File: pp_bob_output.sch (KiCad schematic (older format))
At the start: 24 parts, among them P4 13X2, U1 74LS540, U2 74LVC245, U3 74LS541

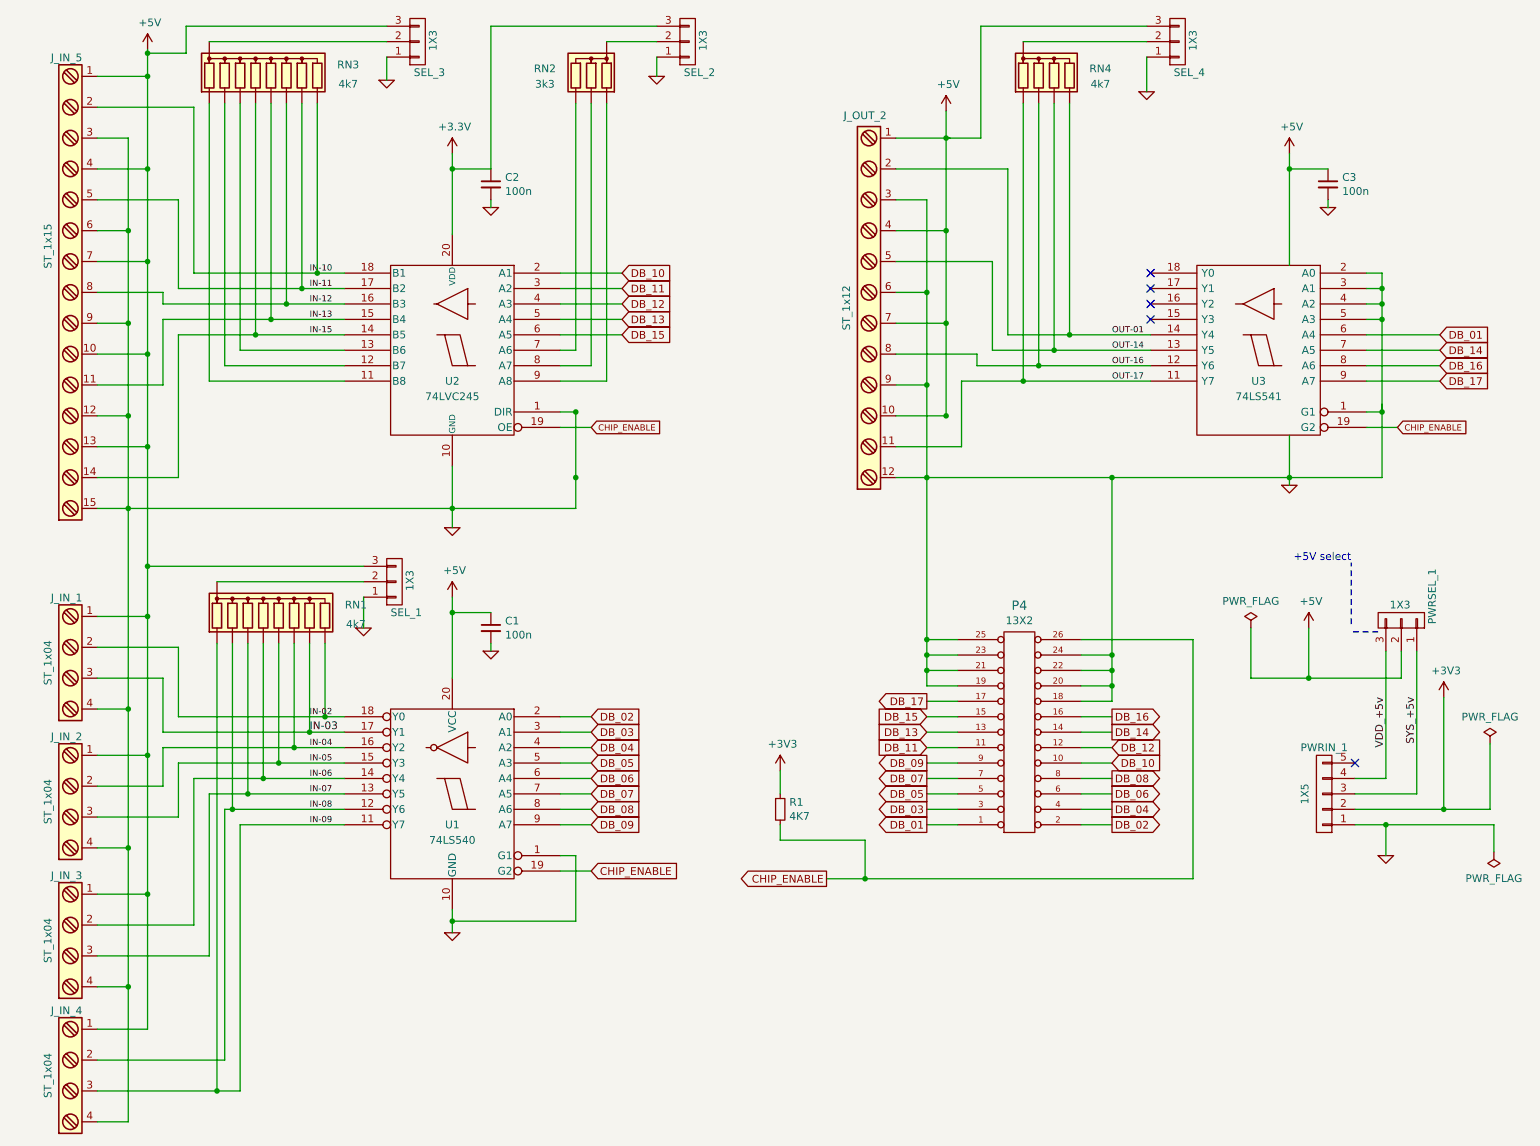
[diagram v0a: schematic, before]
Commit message: Cleaned up schematic
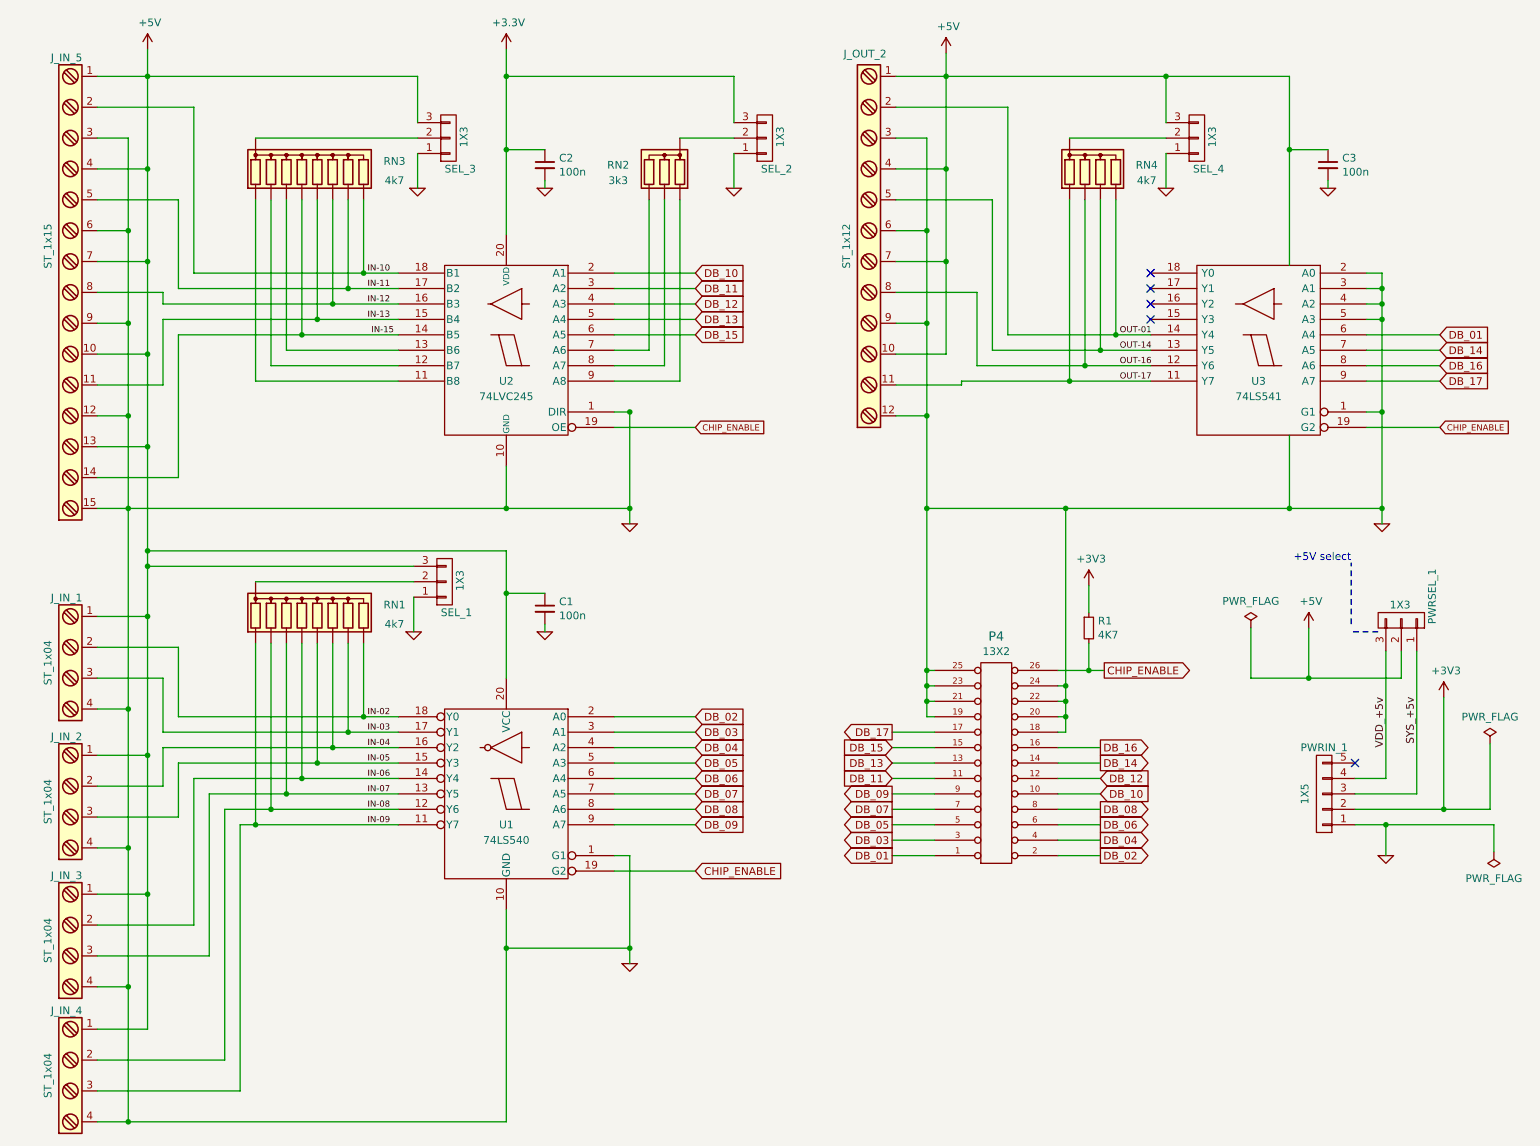
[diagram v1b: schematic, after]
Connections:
- net IN-02: no longer J_IN_1.3, RN1.8 (R7), U1.17 (Y1)
- new net IN-03: J_IN_1.3, RN1.8 (R7), U1.17 (Y1)
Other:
- moved on the sheet: C1, C2, C3, J_OUT_2, P4, R1, RN1, RN2, RN3, RN4, SEL_1, SEL_2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

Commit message: Modified schematic for seperate termianls, PCB modded with terminals spaced equally. Tracks to be rerouted
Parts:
- removed J_IN_5: ST_1x15, w_conn_pt-1,5:pt_1,5-15-3,5-h, symbol Screw_Terminal_1x15
- removed J_OUT_2: ST_1x12, w_conn_pt-1,5:pt_1,5-12-3,5-h, symbol Screw_Terminal_1x12
- added J_IN_1, J_IN_2, J_IN_3, J_IN_4, J_IN_5, J_OUT_5, J_OUT_6, J_OUT_7, J_OUT_8: ST_1x03, w_conn_pt-1,5:pt_1,5-3-3,5-h, symbol Screw_Terminal_1x03
- renumbered J_IN_1 to J_OUT_1, J_IN_2 to J_OUT_2, J_IN_3 to J_OUT_3, J_IN_4 to J_OUT_4
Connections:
- net +5V: now also J_IN_1.1, J_IN_2.1, J_IN_3.1, J_IN_4.1, J_IN_5.1, J_OUT_5.1, J_OUT_6.1, J_OUT_7.1, J_OUT_8.1
- net GND: now also J_IN_1.3, J_IN_2.3, J_IN_3.3, J_IN_4.3, J_IN_5.3, J_OUT_5.3, J_OUT_6.3, J_OUT_7.3, J_OUT_8.3
- net IN-10: now also J_IN_1.2
- net IN-11: now also J_IN_2.2
- net IN-12: now also J_IN_3.2
- net IN-13: now also J_IN_4.2
- net IN-15: now also J_IN_5.2
- net OUT-01: now also J_OUT_5.2
- net OUT-14: now also J_OUT_6.2
- net OUT-16: now also J_OUT_7.2
- net OUT-17: now also J_OUT_8.2
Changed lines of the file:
@@
 $EndComp
 $Comp
-L Screw_Terminal_1x04 J_IN_1
+L Screw_Terminal_1x04 J_OUT_1
 U 1 1 58EEFF7C
 P 1175 4700
-F 0 "J_IN_1" H 1175 5150 50  0000 C TNN
+F 0 "J_OUT_1" H 1175 5150 50  0000 C TNN
 F 1 "ST_1x04" V 1025 4700 50  0000 C TNN
 F 2 "w_conn_pt-1,5:pt_1,5-4-3,5-h" H 1175 4275 50  0001 C CNN
@@
 $EndComp
 $Comp
-L Screw_Terminal_1x04 J_IN_2
+L Screw_Terminal_1x04 J_OUT_2
 U 1 1 58EF0EC1
 P 1175 5600
-F 0 "J_IN_2" H 1175 6050 50  0000 C TNN
+F 0 "J_OUT_2" H 1175 6050 50  0000 C TNN
 F 1 "ST_1x04" V 1025 5600 50  0000 C TNN
 F 2 "w_conn_pt-1,5:pt_1,5-4-3,5-h" H 1175 5175 50  0001 C CNN
@@
 $EndComp
 $Comp
-L Screw_Terminal_1x04 J_IN_3
+L Screw_Terminal_1x04 J_OUT_3
 U 1 1 58EF0F3F
 P 1175 6500
-F 0 "J_IN_3" H 1175 6950 50  0000 C TNN
+F 0 "J_OUT_3" H 1175 6950 50  0000 C TNN
 F 1 "ST_1x04" V 1025 6500 50  0000 C TNN
 F 2 "w_conn_pt-1,5:pt_1,5-4-3,5-h" H 1175 6075 50  0001 C CNN
@@
 $EndComp
 $Comp
-L Screw_Terminal_1x04 J_IN_4
+L Screw_Terminal_1x04 J_OUT_4
 U 1 1 58EF13AB
 P 1175 7375
-F 0 "J_IN_4" H 1175 7825 50  0000 C TNN
+F 0 "J_OUT_4" H 1175 7825 50  0000 C TNN
 F 1 "ST_1x04" V 1025 7375 50  0000 C TNN
 F 2 "w_conn_pt-1,5:pt_1,5-4-3,5-h" H 1175 6950 50  0001 C CNN
@@
 $EndComp
 $Comp
-L Screw_Terminal_1x12 J_OUT_2
-U 1 1 58F01EB1
-P 6350 2000
-F 0 "J_OUT_2" H 6350 3275 50  0000 C TNN
-F 1 "ST_1x12" V 6200 2000 50  0000 C TNN
-F 2 "w_conn_pt-1,5:pt_1,5-12-3,5-h" H 6350 1575 50  0001 C CNN
-F 3 "" H 6325 2200 50  0001 C CNN
-	1    6350 2000
-	1    0    0    -1
-$EndComp
-$Comp
 L +5V #PWR016
 U 1 1 58F01ED5
@@
 NoConn ~ 8200 2275
 NoConn ~ 8200 2175
-$Comp
-L Screw_Terminal_1x15 J_IN_5
-U 1 1 58F030F1
-P 1175 2000
-F 0 "J_IN_5" H 1175 3250 50  0000 C TNN
-F 1 "ST_1x15" V 1025 2000 50  0000 C TNN
-F 2 "w_conn_pt-1,5:pt_1,5-15-3,5-h" H 1175 775 50  0001 C CNN
-F 3 "" H 1150 3000 50  0001 C CNN
-	1    1175 2000
-	1    0    0    -1
-$EndComp
 $Comp
 L R_Network08 RN1
@@
 Connection ~ 4025 6550
 Connection ~ 1575 7675
+$Comp
+L Screw_Terminal_1x03 J_OUT_5
+U 1 1 58FC9F82
+P 6350 1100
+F 0 "J_OUT_5" H 6150 1325 50  0000 C TNN
+F 1 "ST_1x03" V 6200 1000 50  0000 C TNN
+F 2 "w_conn_pt-1,5:pt_1,5-3-3,5-h" H 6350 775 50  0001 C CNN
+F 3 "" H 6325 1200 50  0001 C CNN
+	1    6350 1100
+	1    0    0    -1
+$EndComp
+$Comp
+L Screw_Terminal_1x03 J_OUT_6
+U 1 1 58FCEC7F
+P 6350 1700
+F 0 "J_OUT_6" H 6150 1950 50  0000 C TNN
+F 1 "ST_1x03" V 6200 1600 50  0000 C TNN
+F 2 "w_conn_pt-1,5:pt_1,5-3-3,5-h" H 6350 1375 50  0001 C CNN
+F 3 "" H 6325 1800 50  0001 C CNN
+	1    6350 1700
+	1    0    0    -1
+$EndComp
+$Comp
+L Screw_Terminal_1x03 J_OUT_7
+U 1 1 58FCF132
+P 6350 2300
+F 0 "J_OUT_7" H 6125 2550 50  0000 C TNN
+F 1 "ST_1x03" V 6200 2200 50  0000 C TNN
+F 2 "w_conn_pt-1,5:pt_1,5-3-3,5-h" H 6350 1975 50  0001 C CNN
+F 3 "" H 6325 2400 50  0001 C CNN
+	1    6350 2300
+	1    0    0    -1
+$EndComp
+$Comp
+L Screw_Terminal_1x03 J_OUT_8
+U 1 1 58FCF72A
+P 6350 2900
+F 0 "J_OUT_8" H 6150 3150 50  0000 C TNN
+F 1 "ST_1x03" V 6200 2800 50  0000 C TNN
+F 2 "w_conn_pt-1,5:pt_1,5-3-3,5-h" H 6350 2575 50  0001 C CNN
+F 3 "" H 6325 3000 50  0001 C CNN
+	1    6350 2900
+	1    0    0    -1
+$EndComp
+$Comp
+L Screw_Terminal_1x03 J_IN_1
+U 1 1 58FD9964
+P 1175 1100
+F 0 "J_IN_1" H 975 1325 50  0000 C TNN
+F 1 "ST_1x03" V 1025 1000 50  0000 C TNN
+F 2 "w_conn_pt-1,5:pt_1,5-3-3,5-h" H 1175 775 50  0001 C CNN
+F 3 "" H 1150 1200 50  0001 C CNN
+	1    1175 1100
+	1    0    0    -1
+$EndComp
+$Comp
+L Screw_Terminal_1x03 J_IN_2
+U 1 1 58FD9ABF
+P 1175 1700
+F 0 "J_IN_2" H 975 1925 50  0000 C TNN
+F 1 "ST_1x03" V 1025 1600 50  0000 C TNN
+F 2 "w_conn_pt-1,5:pt_1,5-3-3,5-h" H 1175 1375 50  0001 C CNN
+F 3 "" H 1150 1800 50  0001 C CNN
+	1    1175 1700
+	1    0    0    -1
+$EndComp
+$Comp
+L Screw_Terminal_1x03 J_IN_3
+U 1 1 58FD9B71
+P 1175 2300
+F 0 "J_IN_3" H 975 2525 50  0000 C TNN
+F 1 "ST_1x03" V 1025 2200 50  0000 C TNN
+F 2 "w_conn_pt-1,5:pt_1,5-3-3,5-h" H 1175 1975 50  0001 C CNN
+F 3 "" H 1150 2400 50  0001 C CNN
+	1    1175 2300
+	1    0    0    -1
+$EndComp
+$Comp
+L Screw_Terminal_1x03 J_IN_4
+U 1 1 58FDA2FF
+P 1175 2900
+F 0 "J_IN_4" H 975 3125 50  0000 C TNN
+F 1 "ST_1x03" V 1025 2800 50  0000 C TNN
+F 2 "w_conn_pt-1,5:pt_1,5-3-3,5-h" H 1175 2575 50  0001 C CNN
+F 3 "" H 1150 3000 50  0001 C CNN
+	1    1175 2900
+	1    0    0    -1
+$EndComp
+$Comp
+L Screw_Terminal_1x03 J_IN_5
+U 1 1 58FDA39F
+P 1175 3500
+F 0 "J_IN_5" H 975 3725 50  0000 C TNN
+F 1 "ST_1x03" V 1025 3400 50  0000 C TNN
+F 2 "w_conn_pt-1,5:pt_1,5-3-3,5-h" H 1175 3175 50  0001 C CNN
+F 3 "" H 1150 3600 50  0001 C CNN
+	1    1175 3500
+	1    0    0    -1
+$EndComp
 $EndSCHEMATC

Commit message: Fixed silkscreen & and other details, good for manu
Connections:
- net IN-02 renamed OUT-02
- net IN-03 renamed OUT-03
- net IN-04 renamed OUT-04
- net IN-05 renamed OUT-05
- net IN-06 renamed OUT-06
- net IN-07 renamed OUT-07
- net IN-08 renamed OUT-08
- net IN-09 renamed OUT-09
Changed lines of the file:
@@
 $EndComp
 Text Label 3125 5050 0    40   ~ 0
-IN-02
+OUT-02
 Text Label 3125 5250 0    40   ~ 0
-IN-04
+OUT-04
 Text Label 3125 5350 0    40   ~ 0
-IN-05
+OUT-05
 Text Label 3125 5450 0    40   ~ 0
-IN-06
+OUT-06
 Text Label 3125 5550 0    40   ~ 0
-IN-07
+OUT-07
 Text Label 3125 5650 0    40   ~ 0
-IN-08
+OUT-08
 Text Label 3125 5750 0    40   ~ 0
-IN-09
+OUT-09
 Text GLabel 5250 6050 2    50   Input ~ 0
 CHIP_ENABLE
@@
 $EndComp
 Text Label 3125 5150 0    40   ~ 0
-IN-03
+OUT-03
 Wire Wire Line
 	4725 5950 4825 5950

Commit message: Add docs
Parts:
- U1: symbol 74LS540 -> 74LS540-RESCUE-pp_bob_output
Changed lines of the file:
@@
 EESchema Schematic File Version 2
+LIBS:pp_bob_output-rescue
 LIBS:power
 LIBS:device
@@
 $EndComp
 $Comp
-L 74LS540 U1
+L 74LS540-RESCUE-pp_bob_output U1
 U 1 1 58DDB67C
 P 4025 5550
